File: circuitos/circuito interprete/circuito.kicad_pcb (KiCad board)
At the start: 2 copper layers, 20 parts, among them IC1 ATMEGA328-P, P1 CONN_5V, P10 CONN_LIM_Y, P11 CONN_E_STOP, P2 CONN_02X03, P3 CONN_EJE_X, P4 CONN_EJE_Y, P5 CONN_EJE_Z, P6 CONN_HUS, P7 CONN_UART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

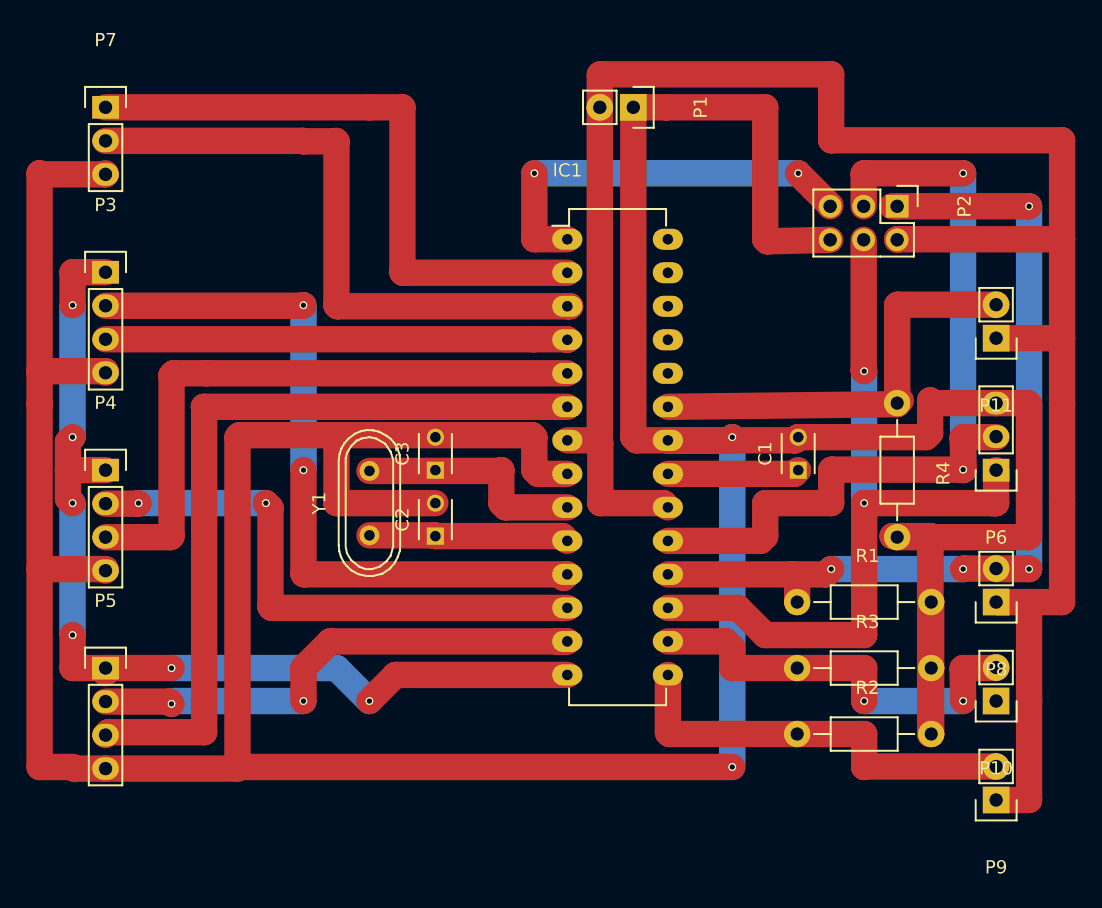
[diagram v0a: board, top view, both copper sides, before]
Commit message: cambios esquematicos varios
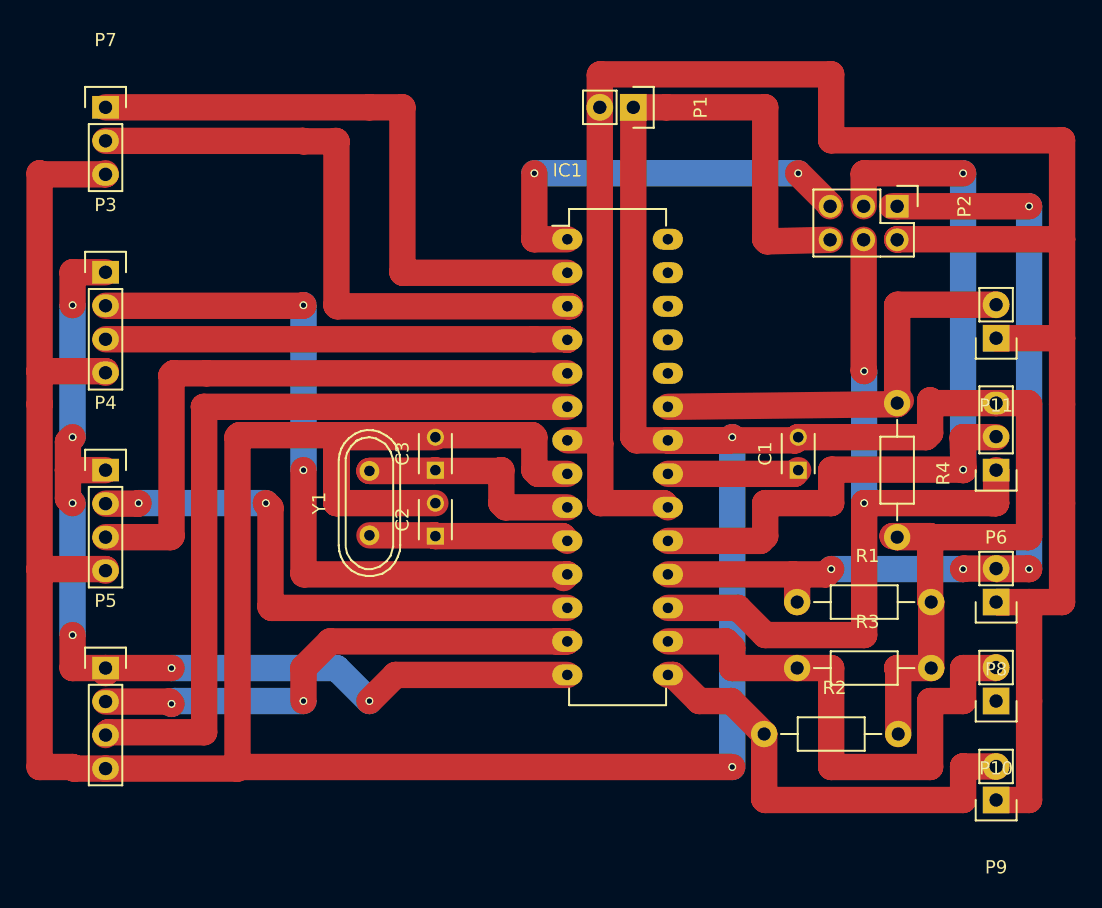
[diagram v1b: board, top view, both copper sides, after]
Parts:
- moved R2 2.50 mm to (177.5, 95.0)
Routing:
- net /lim_Y: track 31.6 -> 41.6 mm, vias 2 -> 0
- net Net-(C3-Pad1): track 17.7 -> 22.7 mm
- net /lim_X: track 31.8 -> 34.3 mm

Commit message: cambios en el circuito de pull down.
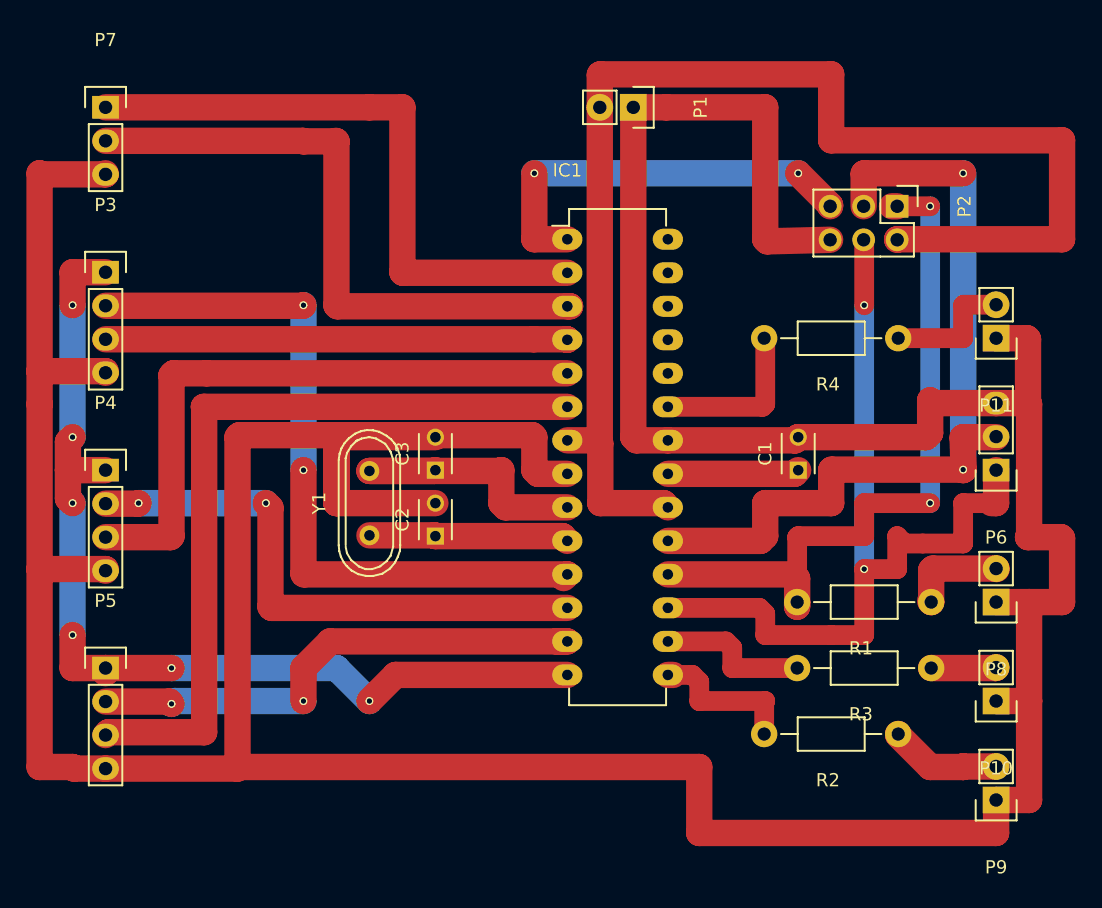
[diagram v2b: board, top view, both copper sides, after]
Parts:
- moved R4 11.2 mm to (177.5, 65.0), turned to 180 degrees
- turned R1 to 180 degrees
- turned R2 to 180 degrees
- turned R3 to 180 degrees
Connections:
- P10 pad 1: VCC -> GND
- P10 pad 2: /lim_Y -> Net-(P10-Pad2)
- P11 pad 1: VCC -> GND
- P11 pad 2: /button_stop -> Net-(P11-Pad2)
- P8 pad 1: VCC -> GND
- P8 pad 2: /MISO -> Net-(P8-Pad2)
- P9 pad 1: VCC -> GND
- P9 pad 2: /lim_X -> Net-(P9-Pad2)
- R1 pad 1: /MISO -> Net-(P8-Pad2)
- R1 pad 2: GND -> /MISO
- R2 pad 1: /lim_X -> Net-(P9-Pad2)
- R2 pad 2: GND -> /lim_X
- R3 pad 1: /lim_Y -> Net-(P10-Pad2)
- R3 pad 2: GND -> /lim_Y
- R4 pad 1: /button_stop -> Net-(P11-Pad2)
- R4 pad 2: GND -> /button_stop
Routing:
- net VCC: track 155.7 -> 100.7 mm
- net /lim_Y: track 41.6 -> 11.5 mm
- net /lim_X: track 34.3 -> 12.0 mm
- net /button_stop: track 32.7 -> 12.5 mm
- net /MISO: track 71.1 -> 54.5 mm, vias 4 -> 2
- net Net-(P11-Pad2): track 0.00 -> 9.94 mm
- net Net-(P9-Pad2): track 0.00 -> 8.58 mm
- net Net-(P8-Pad2): track 0.00 -> 7.56 mm
- net /MOSI: track 58.6 -> 65.4 mm
- net GND: track 346.1 -> 351.9 mm, vias 2 -> 0
- net Net-(P10-Pad2): track 0.00 -> 4.99 mm
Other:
- net class Default: trace_width 2 -> 1.5

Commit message: adapto graficos para el informe
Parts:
- moved P7 2.50 mm to (122.5, 50.0)
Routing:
- net GND: track 351.9 -> 339.2 mm
- net VCC: track 100.7 -> 90.7 mm
- net /Rx_int: track 47.5 -> 45.0 mm
- net /Tx_int: track 47.9 -> 45.5 mm
- net /dir_Z: track 39.3 -> 41.0 mm
- net /enable: track 75.4 -> 73.7 mm
